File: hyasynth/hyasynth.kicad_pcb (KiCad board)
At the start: 2 copper layers, 108 x 53 mm, 41 parts, among them J1 Conn_01x04_Male, J2 Conn_01x02_Male, J3 Conn_01x06_Male, J4 Conn_01x02_Male, J5 Conn_01x04_Male, J6 AudioJack3_SwitchTR, SW1 Power Switch, SW10 G# Ab, SW11 A, SW12 A# Bb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

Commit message: Added Holes for fab
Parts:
- added REF**: MountingHole_1.75mm, MountingHole:MountingHole_1.75mm, F.Cu at (202.8, 42.0)
- added REF**: MountingHole_1.75mm, MountingHole:MountingHole_1.75mm, F.Cu at (261.2, 80.2)
- added REF**: MountingHole_1.75mm, MountingHole:MountingHole_1.75mm, F.Cu at (159.2, 80.2)
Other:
- outline, holes or cut-outs redrawn
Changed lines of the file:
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@@
     )
   )
+  (footprint "MountingHole:MountingHole_1.75mm" (layer "F.Cu")
+    (at 202.75 42)
+    (descr "Mounting Hole 2.1mm, no annular")
+    (tags "mounting hole 2.1mm no annular")
+    (clearance 1)
+    (attr exclude_from_pos_files exclude_from_bom)
+    (fp_text reference "REF**" (at 0 -3.2) (layer "F.SilkS") hide
+      (effects (font (size 1 1) (thickness 0.15)))
+    )
+    (fp_text value "MountingHole_1.75mm" (at 0 3.2) (layer "F.Fab") hide
+      (effects (font (size 1 1) (thickness 0.15)))
+    )
+    (fp_text user "${REFERENCE}" (at 0.1 2.675) (layer "F.Fab") hide
+      (effects (font (size 1 1) (thickness 0.15)))
+    )
+    (fp_circle (center 0 0) (end 1.75 0) (layer "Cmts.User") (width 0.15) (fill none))
+    (fp_circle (center 0 0) (end 2.35 0) (layer "F.CrtYd") (width 0.05) (fill none))
+    (pad "" np_thru_hole circle (at 0 0) (size 3.5 3.5) (drill 3.5) (layers F&B.Cu *.Mask))
+  )
   (footprint "Connector_PinSocket_2.54mm:PinSocket_1x04_P2.54mm_Vertical" (layer "F.Cu")
     (at 218.2 32.8 90)
@@
     )
   )
+  (footprint "MountingHole:MountingHole_1.75mm" (layer "F.Cu")
+    (at 261.2 80.2)
+    (descr "Mounting Hole 2.1mm, no annular")
+    (tags "mounting hole 2.1mm no annular")
+    (attr exclude_from_pos_files exclude_from_bom)
+    (fp_text reference "REF**" (at 0 -3.2) (layer "F.SilkS") hide
+      (effects (font (size 1 1) (thickness 0.15)))
+    )
+    (fp_text value "MountingHole_1.75mm" (at 0 3.2) (layer "F.Fab") hide
+      (effects (font (size 1 1) (thickness 0.15)))
+    )
+    (fp_text user "${REFERENCE}" (at 0.3 0) (layer "F.Fab") hide
+      (effects (font (size 1 1) (thickness 0.15)))
+    )
+    (fp_circle (center 0 0) (end 1.75 0) (layer "Cmts.User") (width 0.15) (fill none))
+    (fp_circle (center 0 0) (end 2.35 0) (layer "F.CrtYd") (width 0.05) (fill none))
+    (pad "" np_thru_hole circle (at 0 0) (size 3.5 3.5) (drill 3.5) (layers F&B.Cu *.Mask)
+      (clearance 1))
+  )
   (footprint "Button:SW_Push_hand_solder" (layer "F.Cu")
     (at 173.2 62.7 180)
@@
     )
   )
+  (footprint "MountingHole:MountingHole_1.75mm" (layer "F.Cu")
+    (at 159.2 80.2)
+    (descr "Mounting Hole 2.1mm, no annular")
+    (tags "mounting hole 2.1mm no annular")
+    (attr exclude_from_pos_files exclude_from_bom)
+    (fp_text reference "REF**" (at 0 -3.2) (layer "F.SilkS") hide
+      (effects (font (size 1 1) (thickness 0.15)))
+    )
+    (fp_text value "MountingHole_1.75mm" (at 0 3.2) (layer "F.Fab") hide
+      (effects (font (size 1 1) (thickness 0.15)))
+    )
+    (fp_text user "${REFERENCE}" (at 0.3 0) (layer "F.Fab") hide
+      (effects (font (size 1 1) (thickness 0.15)))
+    )
+    (fp_circle (center 0 0) (end 1.75 0) (layer "Cmts.User") (width 0.15) (fill none))
+    (fp_circle (center 0 0) (end 2.35 0) (layer "F.CrtYd") (width 0.05) (fill none))
+    (pad "" np_thru_hole circle (at 0 0) (size 3.5 3.5) (drill 3.5) (layers F&B.Cu *.Mask)
+      (clearance 1))
+  )
   (footprint "Button:SW_Push_hand_solder" (layer "F.Cu")
     (at 181.2 37.2)
@@
   (gr_circle (center 159.1 80.15) (end 157.1 80.15) (layer "Dwgs.User") (width 0.2) (fill none))
   (gr_line locked (start 209.95 66.45) (end 204.45 66.45) (layer "Dwgs.User") (width 0.2))
-  (gr_circle (center 203.25 42) (end 206.25 42) (layer "Dwgs.User") (width 0.15) (fill none))
   (gr_line locked (start 262.2 20.2) (end 262.2 81.2) (layer "Dwgs.User") (width 0.2))
   (gr_line locked (start 218.95 65.95) (end 218.95 46.2) (layer "Dwgs.User") (width 0.2))
@@
   (gr_line locked (start 169.7 46.2) (end 176.7 46.2) (layer "Dwgs.User") (width 0.2))
   (gr_rect (start 156.25 30.2) (end 264.25 83.25) (layer "Edge.Cuts") (width 0.1) (fill none))
-  (gr_circle (center 202.75 42) (end 204.5 42) (layer "Edge.Cuts") (width 0.1) (fill none))
-  (gr_circle (center 261.2 80.2) (end 262.95 80.2) (layer "Edge.Cuts") (width 0.1) (fill none))
-  (gr_circle (center 159.2 80.2) (end 160.95 80.2) (layer "Edge.Cuts") (width 0.1) (fill none))
   (gr_circle (center 202.75 42) (end 206.25 42) (layer "User.3") (width 0.15) (fill none))
   (gr_text "GPIO" (at 185.375 32.875) (layer "B.SilkS")
@@
   (segment (start 257.35 50.95) (end 257.35 45.9) (width 0.508) (layer "F.Cu") (net 40))
   (segment (start 255.875 44.425) (end 251.275 44.425) (width 0.508) (layer "F.Cu") (net 40))
-  (zone (net 0) (net_name "") (layers F&B.Cu) (hatch edge 0.508)
-    (connect_pads (clearance 0))
-    (min_thickness 0.254)
-    (keepout (tracks not_allowed) (vias not_allowed) (pads not_allowed ) (copperpour not_allowed) (footprints not_allowed))
-    (fill (thermal_gap 0.508) (thermal_bridge_width 0.508))
-    (polygon
-      (pts
-        (xy 204.25 39.25)
-        (xy 205.5 40)
-        (xy 206.25 41.25)
-        (xy 206.25 42.5)
-        (xy 205.75 43.5)
-        (xy 205.25 44.25)
-        (xy 205 44.5)
-        (xy 203.5 45)
-        (xy 202.75 45)
-        (xy 201.5 44.5)
-        (xy 200.75 43.75)
-        (xy 200.25 42.75)
-        (xy 200.25 41.5)
-        (xy 201 40)
-        (xy 202 39.25)
-        (xy 203.25 39)
-      )
-    )
-  )
   (zone (net 3) (net_name "GND") (layer "F.Cu") (hatch edge 0.508)
     (connect_pads (clearance 0.508))
@@
     )
   )
-  (zone (net 0) (net_name "") (layers F&B.Cu) (hatch edge 0.508)
-    (connect_pads (clearance 0))
-    (min_thickness 0.254)
-    (keepout (tracks not_allowed) (vias not_allowed) (pads not_allowed ) (copperpour not_allowed) (footprints allowed))
-    (fill (thermal_gap 0.508) (thermal_bridge_width 0.508))
-    (polygon
-      (pts
-        (xy 263 83.25)
-        (xy 258.1 83.2)
-        (xy 258 77)
-        (xy 263 77)
-      )
-    )
-  )
   (zone (net 0) (net_name "") (layer "F.Cu") (hatch edge 0.508)
     (connect_pads (clearance 0))
@@
       )
     )
-  )
-  (zone (net 0) (net_name "") (layers F&B.Cu) (hatch edge 0.508)
-    (connect_pads (clearance 0))
-    (min_thickness 0.254)
-    (keepout (tracks not_allowed) (vias not_allowed) (pads not_allowed ) (copperpour not_allowed) (footprints allowed))
-    (fill (thermal_gap 0.508) (thermal_bridge_width 0.508))
-    (polygon
-      (pts
-        (xy 162.5 83)
-        (xy 157.4 83)
-        (xy 157.5 76.75)
-        (xy 162.5 76.75)
-      )
-    )

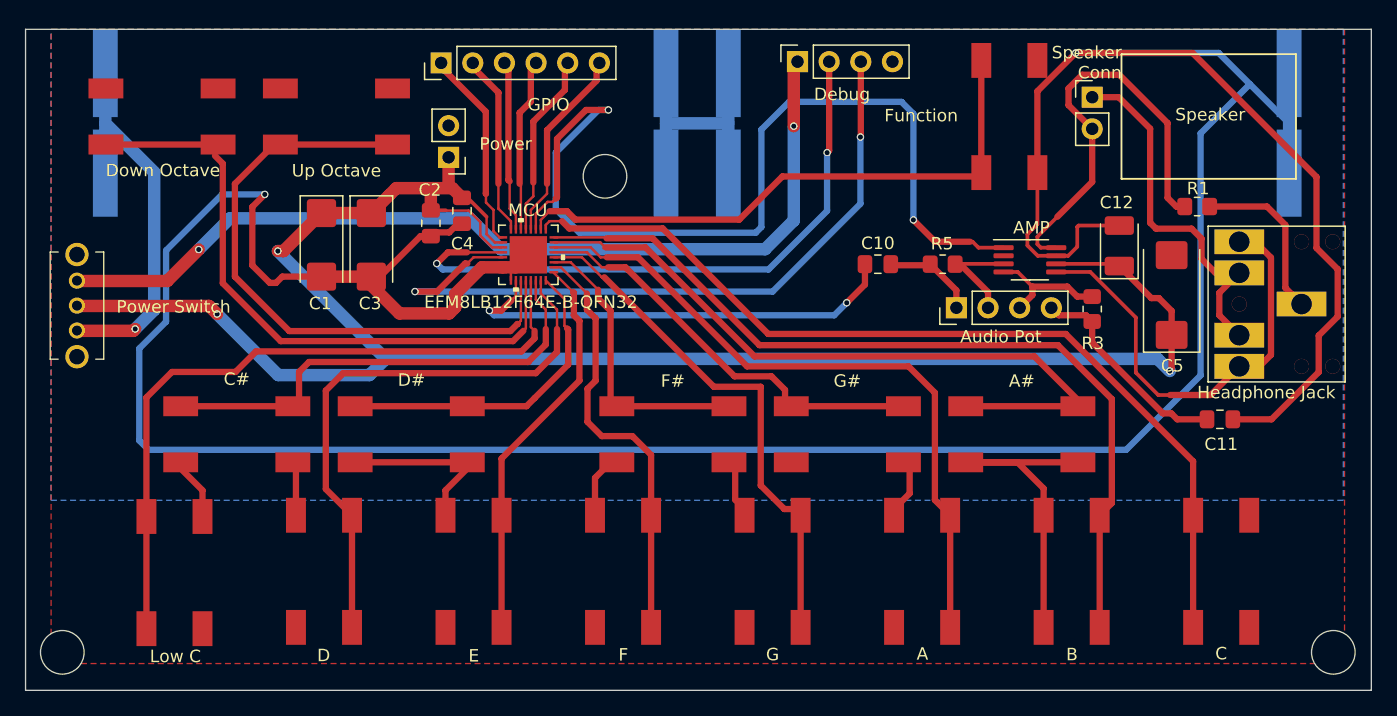
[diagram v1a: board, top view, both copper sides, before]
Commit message: adjusted battery silkscreen position and edge cut for andrew
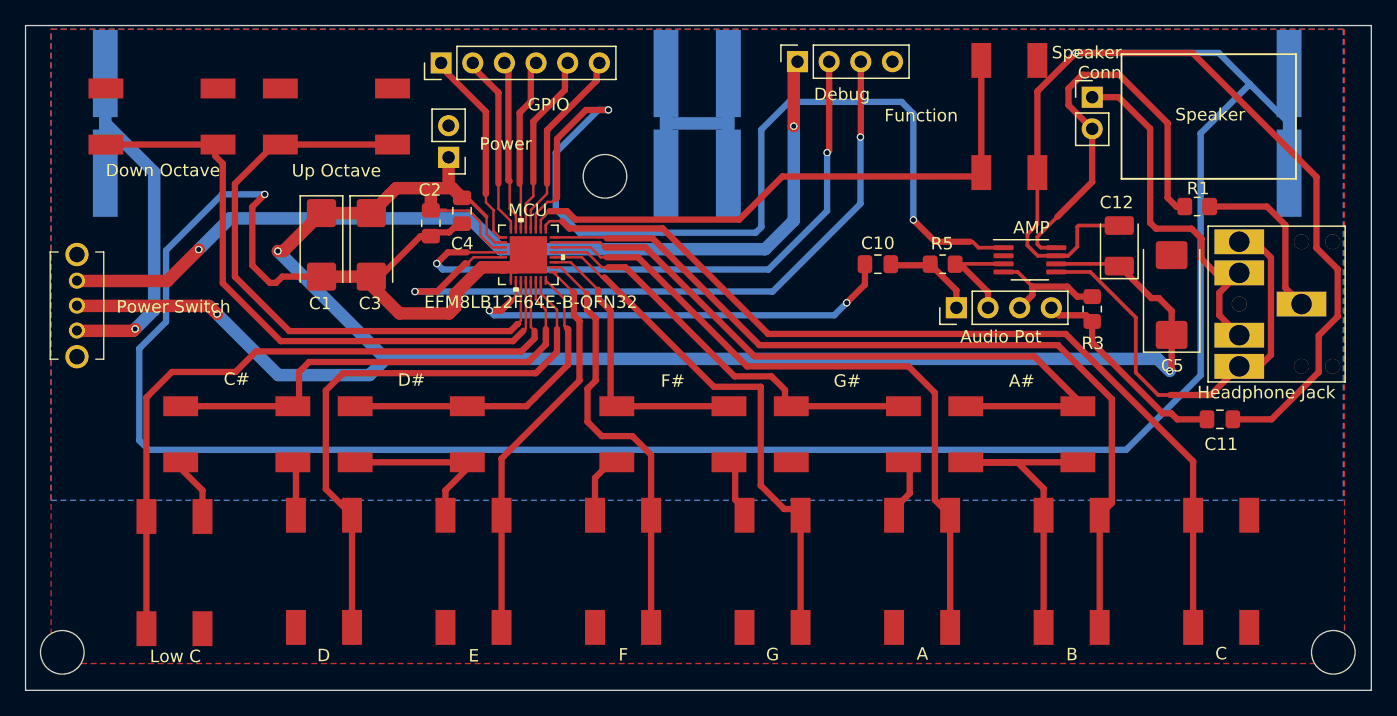
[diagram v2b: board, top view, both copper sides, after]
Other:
- board size 108 x 53 mm -> 108 x 53.4 mm
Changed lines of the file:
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@@
     (property "Sheetname" "")
     (attr smd)
-    (fp_text reference "BT2" (at -0.15 -9.5 unlocked) (layer "B.SilkS")
+    (fp_text reference "BT2" (at 17.55 -6.35 unlocked) (layer "B.SilkS")
       (effects (font (size 1 1) (thickness 0.15)) (justify mirror))
     )
@@
     (property "Sheetname" "")
     (attr smd)
-    (fp_text reference "BT1" (at -0.15 -11.65 unlocked) (layer "B.SilkS")
+    (fp_text reference "BT1" (at -17.45 -6.25 unlocked) (layer "B.SilkS")
       (effects (font (size 1 1) (thickness 0.15)) (justify mirror))
     )
@@
   (gr_line locked (start 177.199999 33.199999) (end 177.647213 32.305573) (layer "Dwgs.User") (width 0.2))
   (gr_line locked (start 169.7 46.2) (end 176.7 46.2) (layer "Dwgs.User") (width 0.2))
-  (gr_rect (start 156.25 30.2) (end 264.25 83.25) (layer "Edge.Cuts") (width 0.1) (fill none))
+  (gr_rect (start 156.25 29.9) (end 264.25 83.25) (layer "Edge.Cuts") (width 0.1) (fill none))
   (gr_circle (center 202.75 42) (end 206.25 42) (layer "User.3") (width 0.15) (fill none))
   (gr_text "GPIO" (at 185.375 32.875) (layer "B.SilkS")
